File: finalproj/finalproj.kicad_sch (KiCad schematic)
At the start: 34 parts, among them J10 Motor Out B, J11 Motor Out A, J5 Stepper_Motor_Controller, J7 LIDAR_Connector, J9 RPI_UART_Conn, U2 LM1085-12, U3 LM1085-5.0, U4 LM1085-3.3, U5 L298N

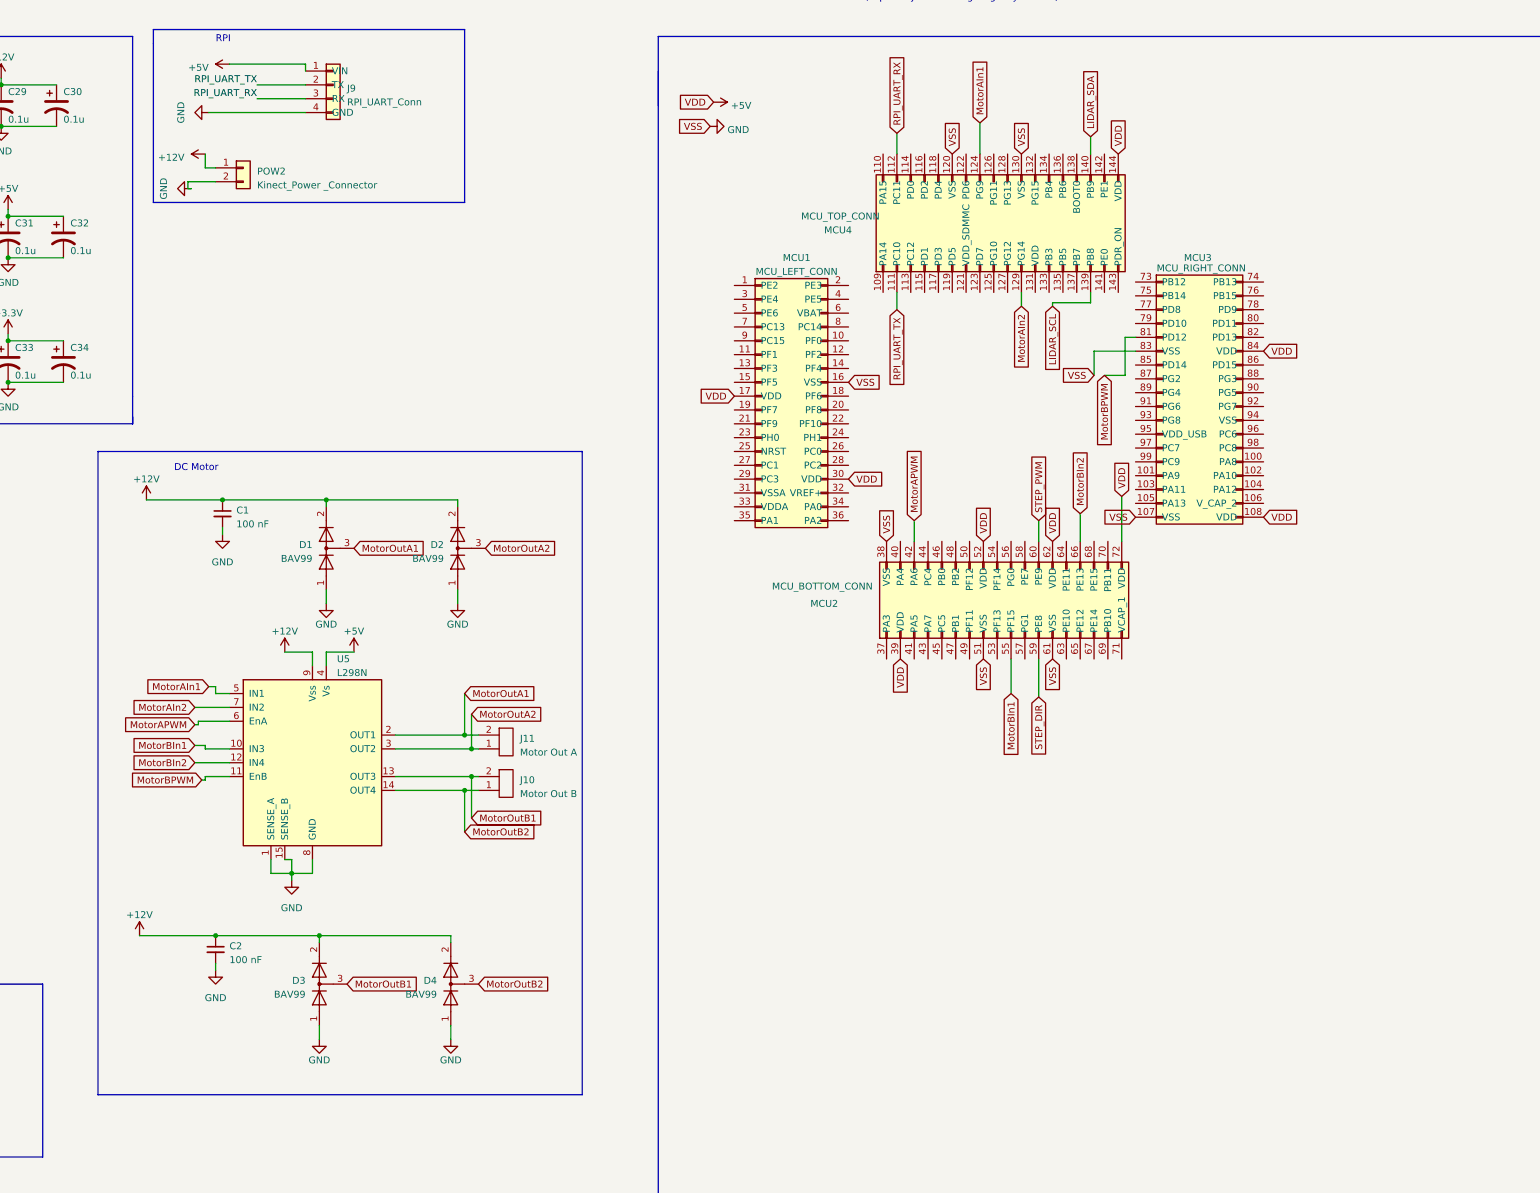
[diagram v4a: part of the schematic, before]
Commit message: resized the board and fixed errors
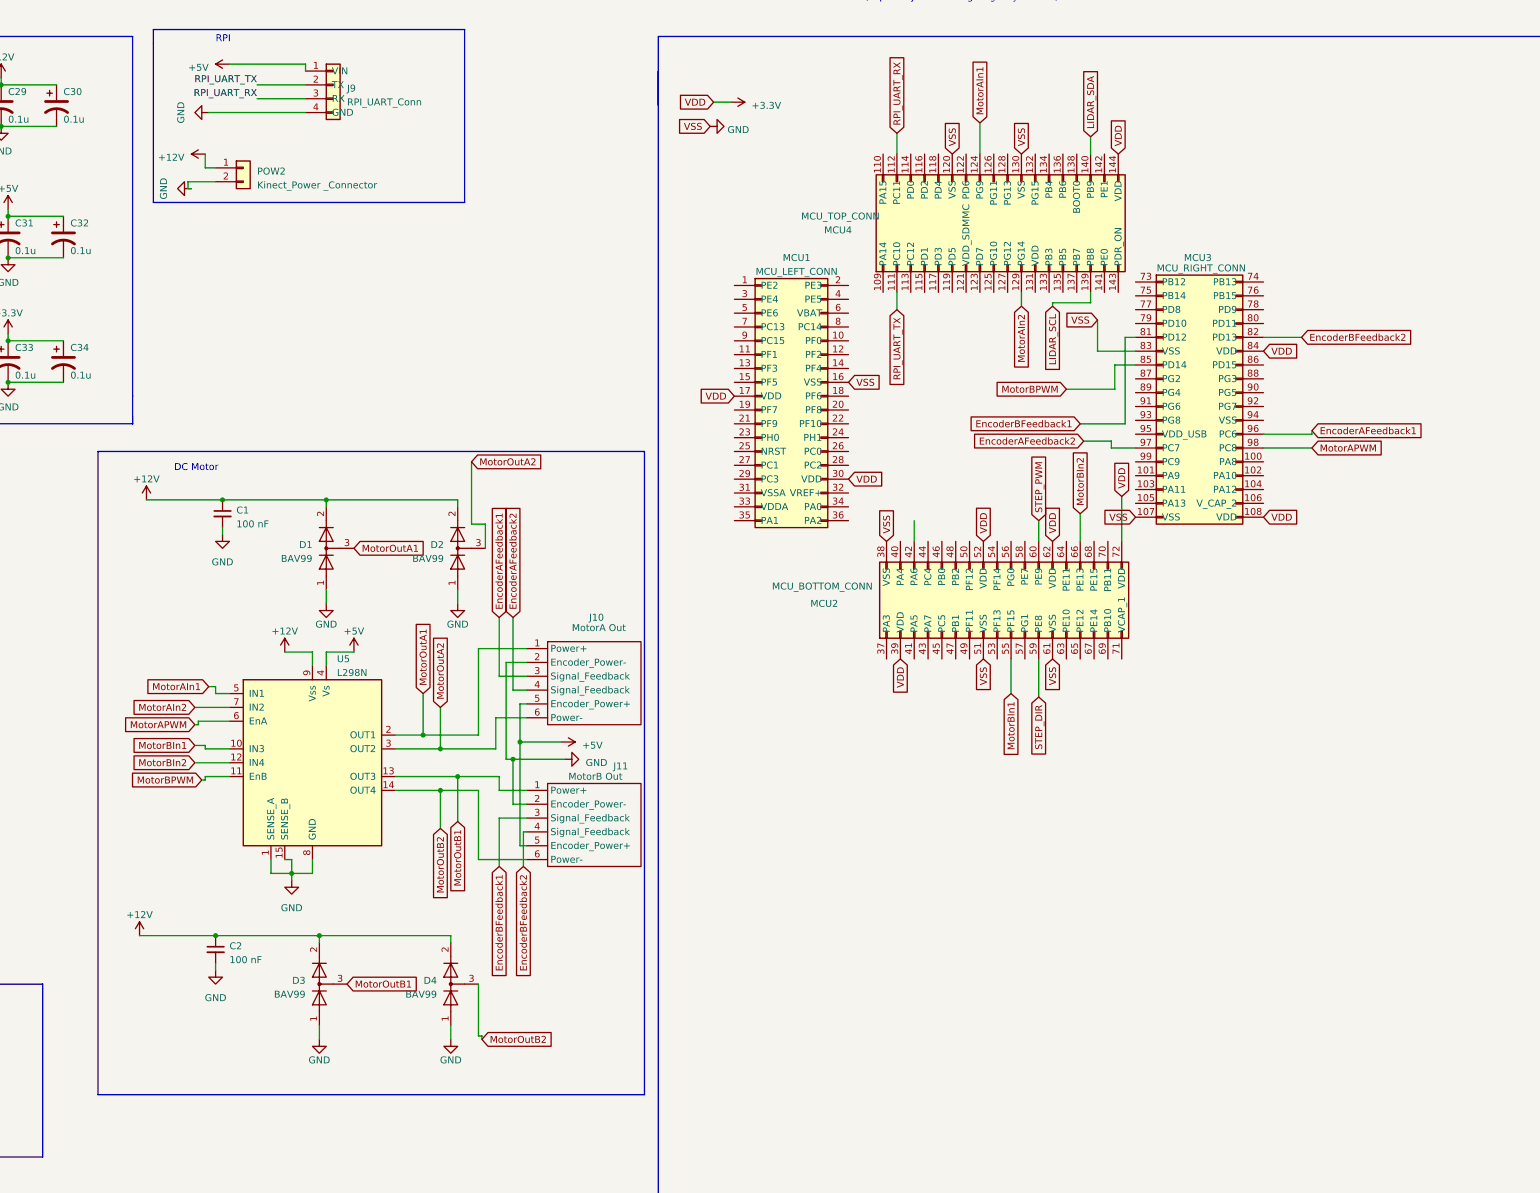
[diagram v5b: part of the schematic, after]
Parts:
- J10: renamed from J11; value Motor Out A -> MotorA Out; footprint TerminalBlock_Phoenix:TerminalBlock_Phoenix_PT-1,5-2-5.0-H_1x02_P5.00mm_Horizontal -> TerminalBlock_Phoenix:TerminalBlock_Phoenix_PT-1,5-6-3.5-H_1x06_P3.50mm_Horizontal
- J11: renamed from J10; value Motor Out B -> MotorB Out; footprint TerminalBlock_Phoenix:TerminalBlock_Phoenix_PT-1,5-2-5.0-H_1x02_P5.00mm_Horizontal -> TerminalBlock_Phoenix:TerminalBlock_Phoenix_PT-1,5-6-3.5-H_1x06_P3.50mm_Horizontal
- U5: footprint Package_TO_SOT_THT:TO-220-15_P2.54x2.54mm_StaggerOdd_Lead5.84mm_TabDown -> Package_TO_SOT_THT:TO-220-15_P2.54x2.54mm_StaggerOdd_Lead4.58mm_Vertical
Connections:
- net +3.3V: now also MCU1.17 (VDD), MCU1.30 (VDD), MCU2.39 (VDD), MCU2.52 (VDD), MCU2.62 (VDD), MCU2.72 (VDD), MCU3.108 (VDD), MCU3.84 (VDD), MCU4.144 (VDD)
- net +5V: now also J10.5 (Encoder_Power+), J11.5 (Encoder_Power+); no longer MCU1.17 (VDD), MCU1.30 (VDD), MCU2.39 (VDD), MCU2.52 (VDD), MCU2.62 (VDD), MCU2.72 (VDD), MCU3.108 (VDD), MCU3.84 (VDD), MCU4.144 (VDD)
- net GND: now also J10.2 (Encoder_Power-), J11.2 (Encoder_Power-)
- net MotorAPWM: now also MCU3.98 (PC8); no longer MCU2.42 (PA6)
- net MotorBPWM: now also MCU3.85 (PD14); no longer MCU3.81 (PD12)
- net MotorOutA1: now also J10.1 (Power+); no longer J10.2 (Out-)
- net MotorOutA2: now also J10.6 (Power-); no longer J10.1 (Out+)
- net MotorOutB1: now also J11.1 (Power+); no longer J11.2 (Out-)
- net MotorOutB2: now also J11.6 (Power-); no longer J11.1 (Out+)
- net EncoderBFeedback2: now reaches MCU3.82 (PD13)
- net EncoderBFeedback2: now also J11.4 (Signal_Feedback)
- net EncoderAFeedback1: now reaches MCU3.96 (PC6)
- net EncoderAFeedback1: now also J10.3 (Signal_Feedback)
- net EncoderAFeedback2: now reaches MCU3.97 (PC7)
- net EncoderAFeedback2: now also J10.4 (Signal_Feedback)
- new net EncoderBFeedback1: J11.3 (Signal_Feedback), MCU3.81 (PD12)

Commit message: main pcb is completed no warnings
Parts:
- MCU1: footprint Connector_PinSocket_2.54mm:PinSocket_2x18_P2.54mm_Vertical -> MCU_SOCKETS:MCU1_SOCKET
- MCU2: footprint Connector_PinSocket_2.54mm:PinSocket_2x18_P2.54mm_Vertical -> MCU_SOCKETS:MCU2_SOCKETS
- MCU3: footprint Connector_PinSocket_2.54mm:PinSocket_2x18_P2.54mm_Vertical -> MCU_SOCKETS:MCU3_SOCKETS
- MCU4: footprint Connector_PinSocket_2.54mm:PinSocket_2x18_P2.54mm_Vertical -> MCU_SOCKETS:MCU4_SOCKETS
- POW2: footprint TerminalBlock_Phoenix:TerminalBlock_Phoenix_PT-1,5-2-5.0-H_1x02_P5.00mm_Horizontal -> TerminalBlock_Phoenix:TerminalBlock_Phoenix_PT-1,5-2-3.5-H_1x02_P3.50mm_Horizontal
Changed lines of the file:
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@@
       (effects (font (size 1.27 1.27)) (justify left))
     )
-    (property "Footprint" "TerminalBlock_Phoenix:TerminalBlock_Phoenix_PT-1,5-2-5.0-H_1x02_P5.00mm_Horizontal" (at 124.46 38.1 0)
+    (property "Footprint" "TerminalBlock_Phoenix:TerminalBlock_Phoenix_PT-1,5-2-3.5-H_1x02_P3.50mm_Horizontal" (at 124.46 38.1 0)
       (effects (font (size 1.27 1.27)) hide)
     )
@@
       (effects (font (size 1.27 1.27)))
     )
-    (property "Footprint" "Connector_PinSocket_2.54mm:PinSocket_2x18_P2.54mm_Vertical" (at 293.37 79.375 0)
+    (property "Footprint" "MCU_SOCKETS:MCU3_SOCKETS" (at 293.37 79.375 0)
       (effects (font (size 1.27 1.27)) hide)
     )
@@
       (effects (font (size 1.27 1.27)) (justify left))
     )
-    (property "Footprint" "Connector_PinSocket_2.54mm:PinSocket_2x18_P2.54mm_Vertical" (at 262.255 55.88 0)
+    (property "Footprint" "MCU_SOCKETS:MCU4_SOCKETS" (at 262.255 55.88 0)
       (effects (font (size 1.27 1.27)) hide)
     )
@@
       (effects (font (size 1.27 1.27)))
     )
-    (property "Footprint" "Connector_PinSocket_2.54mm:PinSocket_2x18_P2.54mm_Vertical" (at 219.71 80.01 0)
+    (property "Footprint" "MCU_SOCKETS:MCU1_SOCKET" (at 219.71 80.01 0)
       (effects (font (size 1.27 1.27)) hide)
     )
@@
       (effects (font (size 1.27 1.27)) (justify left))
     )
-    (property "Footprint" "Connector_PinSocket_2.54mm:PinSocket_2x18_P2.54mm_Vertical" (at 262.89 123.19 0)
-      (effects (font (size 1.27 1.27)) hide)
-    )
+    (property "Footprint" "MCU_SOCKETS:MCU2_SOCKETS" (at 262.89 123.19 0)
+      (effects (font (size 1.27 1.27)) hide)
+    )

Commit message: finished pcb, pcbway confirmed
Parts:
- added C3, C5, C6: 0.1u, Capacitor_SMD:C_0805_2012Metric, symbol Device:C_Polarized_US
- added C4: 0.47u, Capacitor_SMD:C_0805_2012Metric, symbol Device:C_Polarized_US
- added H1, H2, H3, H4: MountingHole, MountingHole:MountingHole_3.2mm_M3, symbol Mechanical:MountingHole
- added U1: LM1085-12, LM1085IT-5.0:TO254P1054X470X1955-3, symbol Regulator_Linear:LM1085-12
- J7: footprint Connector_Phoenix_MC:PhoenixContact_MCV_1,5_6-G-3.81_1x06_P3.81mm_Vertical -> Connector_PinHeader_2.54mm:PinHeader_1x06_P2.54mm_Vertical
- J9: footprint Connector_Phoenix_MC:PhoenixContact_MCV_1,5_4-G-3.81_1x04_P3.81mm_Vertical -> Connector_PinHeader_2.54mm:PinHeader_1x04_P2.54mm_Vertical
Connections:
- net +12V: no longer POW2.1 (VIN)
- net GND: now also MCU4.138 (BOOT0), C3.2, C4.2, C5.2, C6.2, U1.1 (GND)
- net BATTERY_VIN: now reaches C24.1, C25.1, C35.1, POW1.2 (Pin_2), U2.3 (VI), U3.3 (VI), U4.3 (VI)
- net BATTERY_VIN: now also C4.1, U1.3 (VI)
- new net 12V_IC: C3.1, C5.1, C6.1, POW2.1 (VIN), U1.2 (VO)
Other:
- moved on the sheet: POW2, POW3

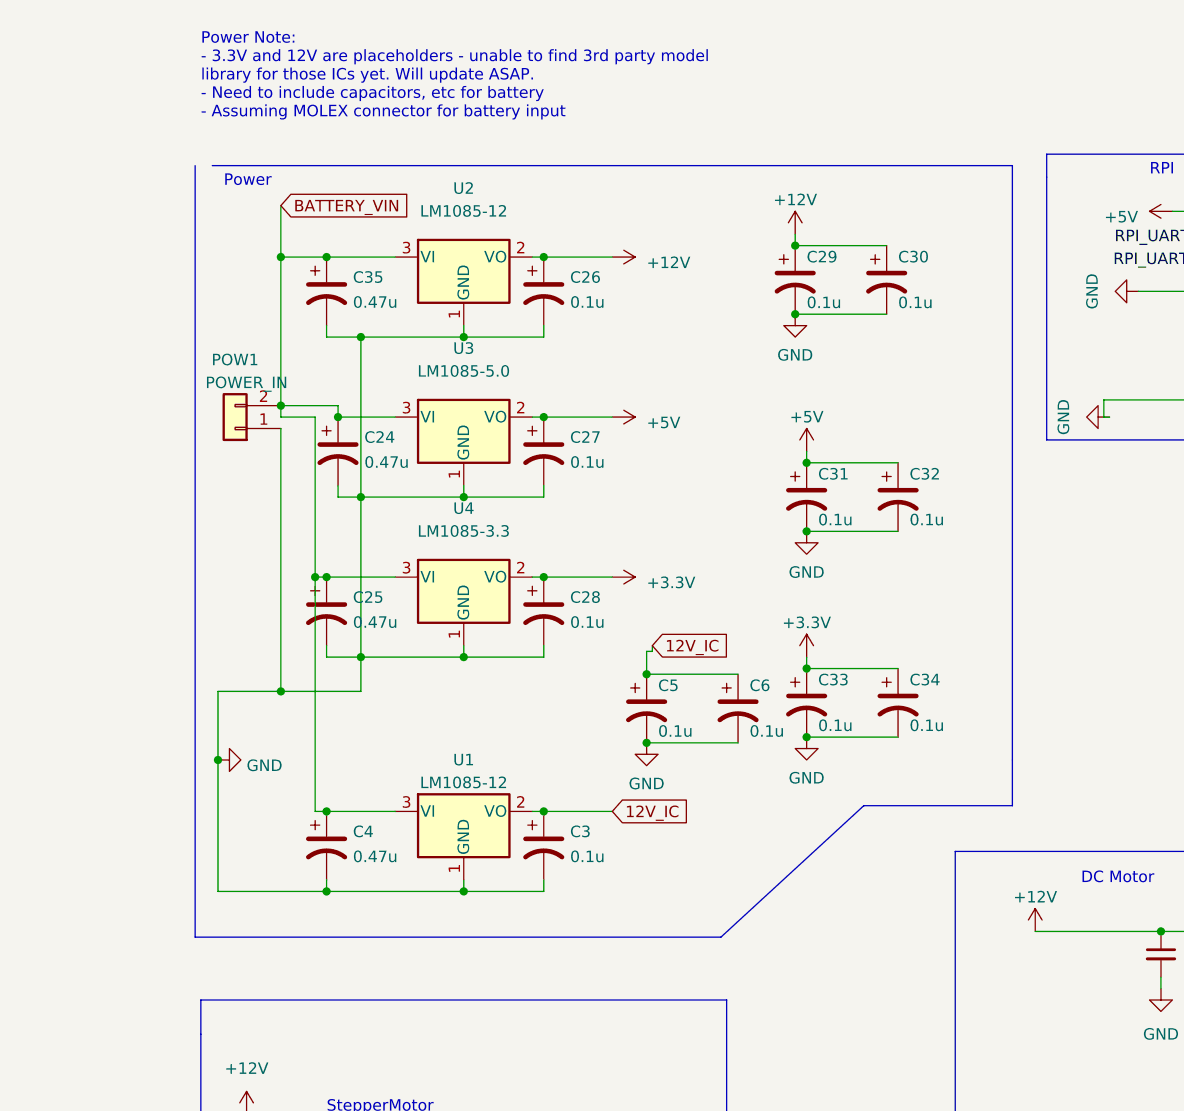
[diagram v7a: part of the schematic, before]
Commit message: added resistors
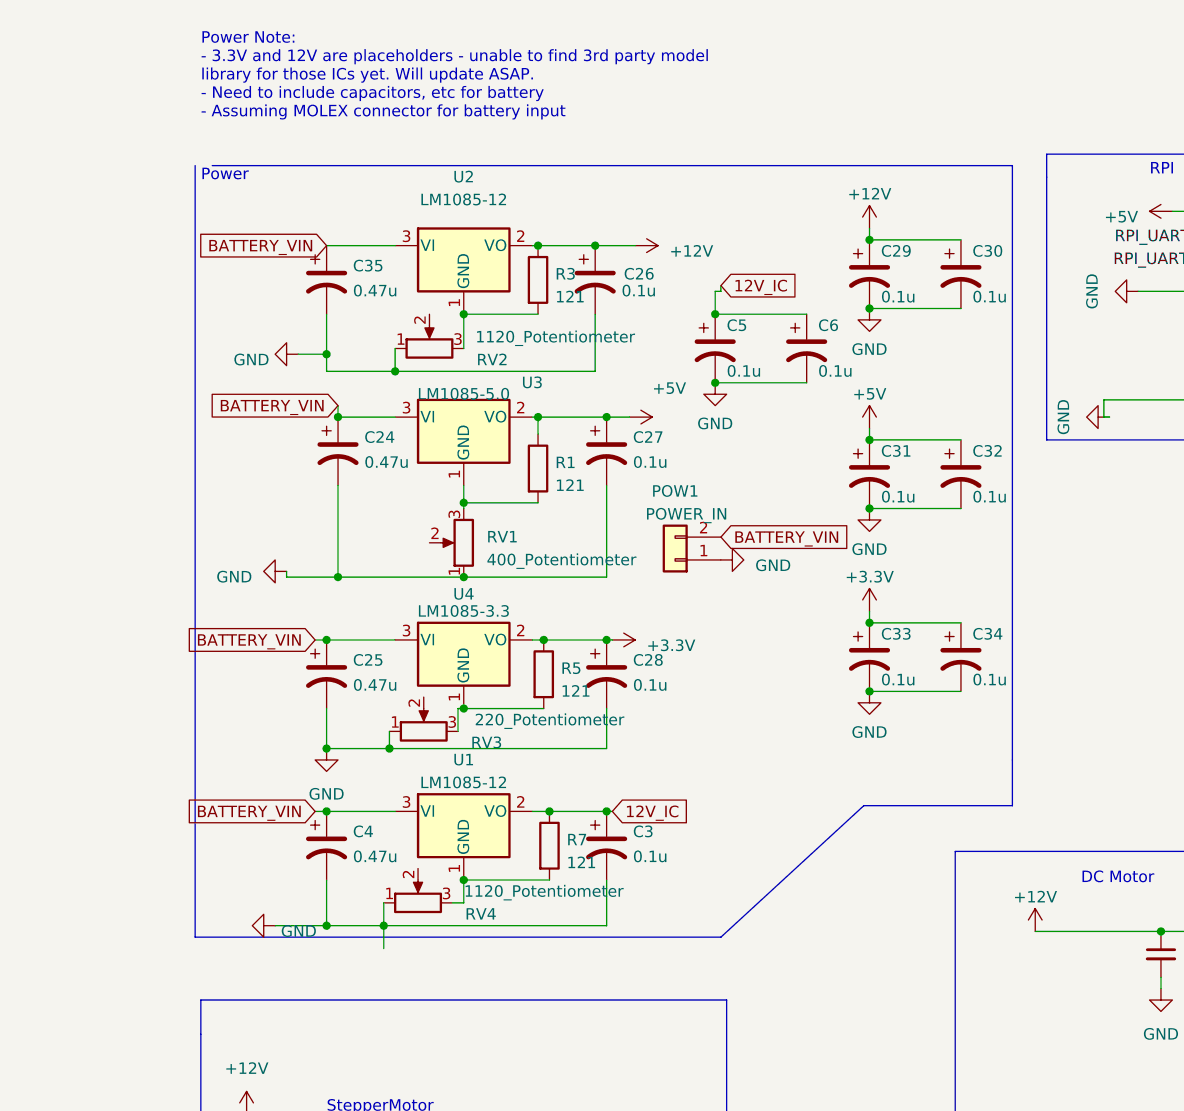
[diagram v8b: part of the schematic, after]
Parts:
- added R1, R3, R5, R7: 121, Resistor_SMD:R_1206_3216Metric_Pad1.30x1.75mm_HandSolder, symbol Device:R
- added RV1: 400_Potentiometer, Potentiometer_SMD:Potentiometer_Bourns_TC33X_Vertical, symbol Device:R_Potentiometer
- added RV2, RV4: 1120_Potentiometer, Potentiometer_SMD:Potentiometer_Bourns_TC33X_Vertical, symbol Device:R_Potentiometer
- added RV3: 220_Potentiometer, Potentiometer_SMD:Potentiometer_Bourns_TC33X_Vertical, symbol Device:R_Potentiometer
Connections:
- net +12V: now also R3.1
- net +3.3V: now also R5.1
- net +5V: now also R1.1
- net 12V_IC: now also R7.1
- net GND: now also RV1.1, RV2.1, RV3.1, RV4.1; no longer U1.1 (GND), U2.1 (GND), U3.1 (GND), U4.1 (GND)
- new net: R7.2, RV4.3, U1.1 (GND)
- new net: R1.2, RV1.3, U3.1 (GND)
- new net: R3.2, RV2.3, U2.1 (GND)
- new net: R5.2, RV3.3, U4.1 (GND)
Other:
- moved on the sheet: C25, C26, C27, C28, C29, C3, C30, C31, C32, C33, C34, C35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
